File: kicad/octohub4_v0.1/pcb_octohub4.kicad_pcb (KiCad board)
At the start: 2 copper layers, 100 x 80 mm, 83 parts, among them J101 USB231ARY, J102 USB231ARY, J103 USB231ARY, J104 USB231ARY, J201 Screw_Terminal_01x02, J203 Barrel_Jack_Switch, J301 USB_C_Receptacle_USB2.0, U201 TPS259474LRPWR, U301 AMS1117-3.3, U302 USB2514B_Bi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

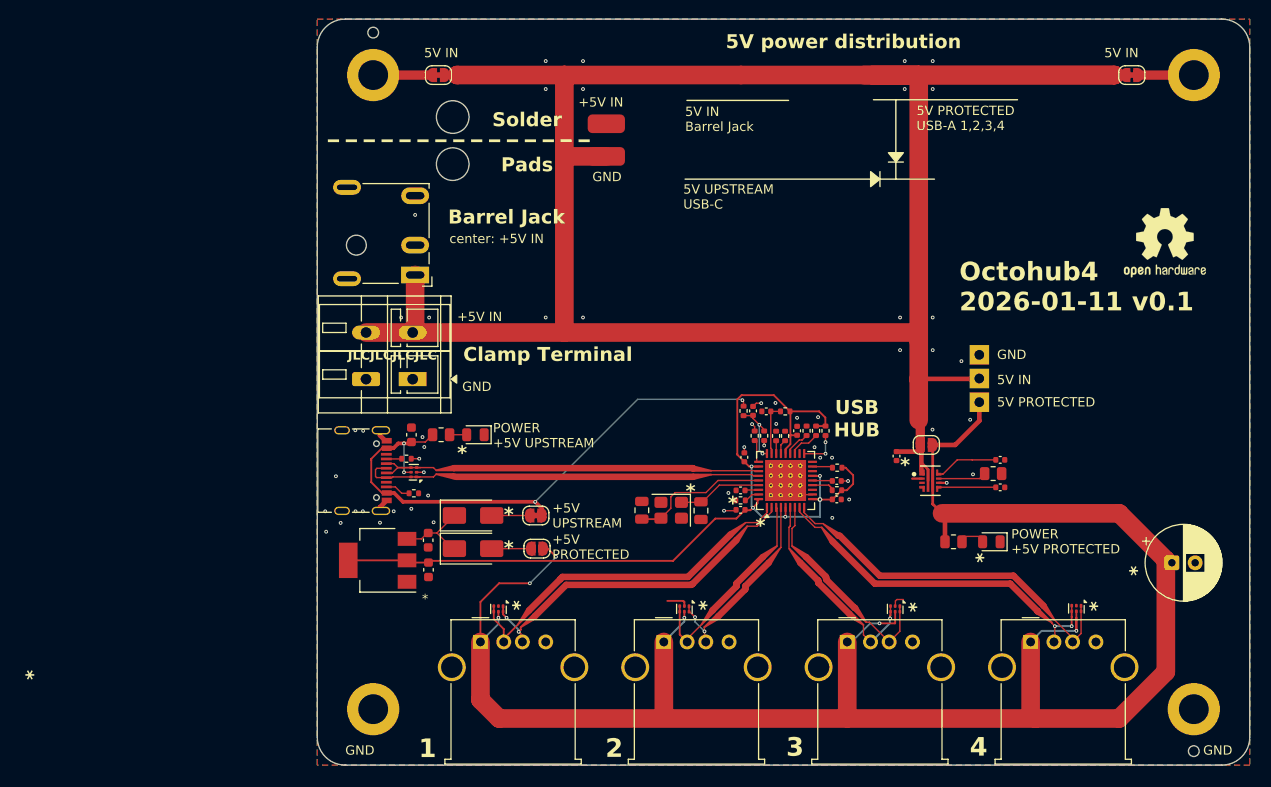
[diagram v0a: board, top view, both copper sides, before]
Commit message: Add run_kicad_purge 6
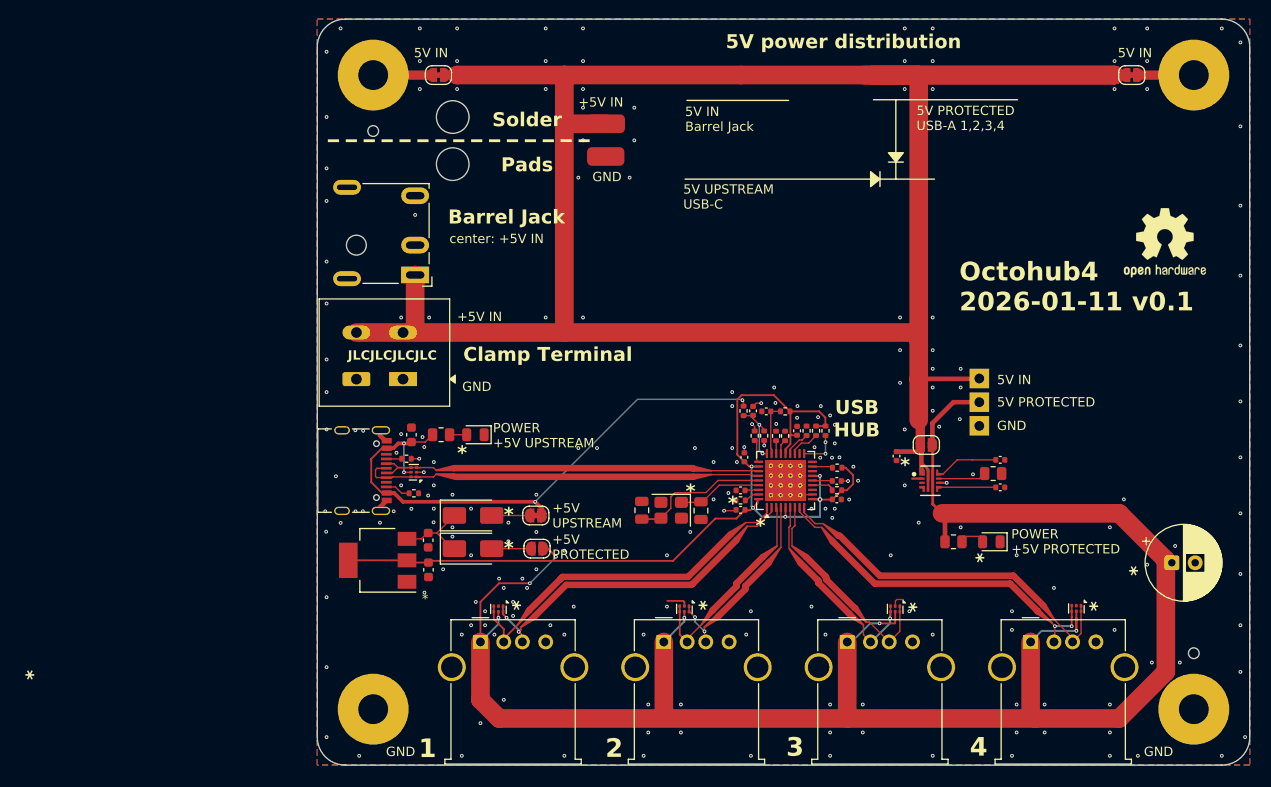
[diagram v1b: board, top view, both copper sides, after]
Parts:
- moved TH1301 10.6 mm to (64.8, 29.3)
- moved TH1302 10.5 mm to (152.8, 85.3)
- moved BP203 7.62 mm to (129.8, 60.9)
- moved BP202 3.51 mm to (89.7, 32.0)
- moved BP201 3.50 mm to (89.8, 28.5)
- moved J201 1.03 mm to (63.0, 55.9)
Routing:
- net +5VIN: track 255.4 -> 256.6 mm
- net GND: vias 55 -> 216
